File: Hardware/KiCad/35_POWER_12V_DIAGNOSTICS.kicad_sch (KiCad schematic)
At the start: 0 parts

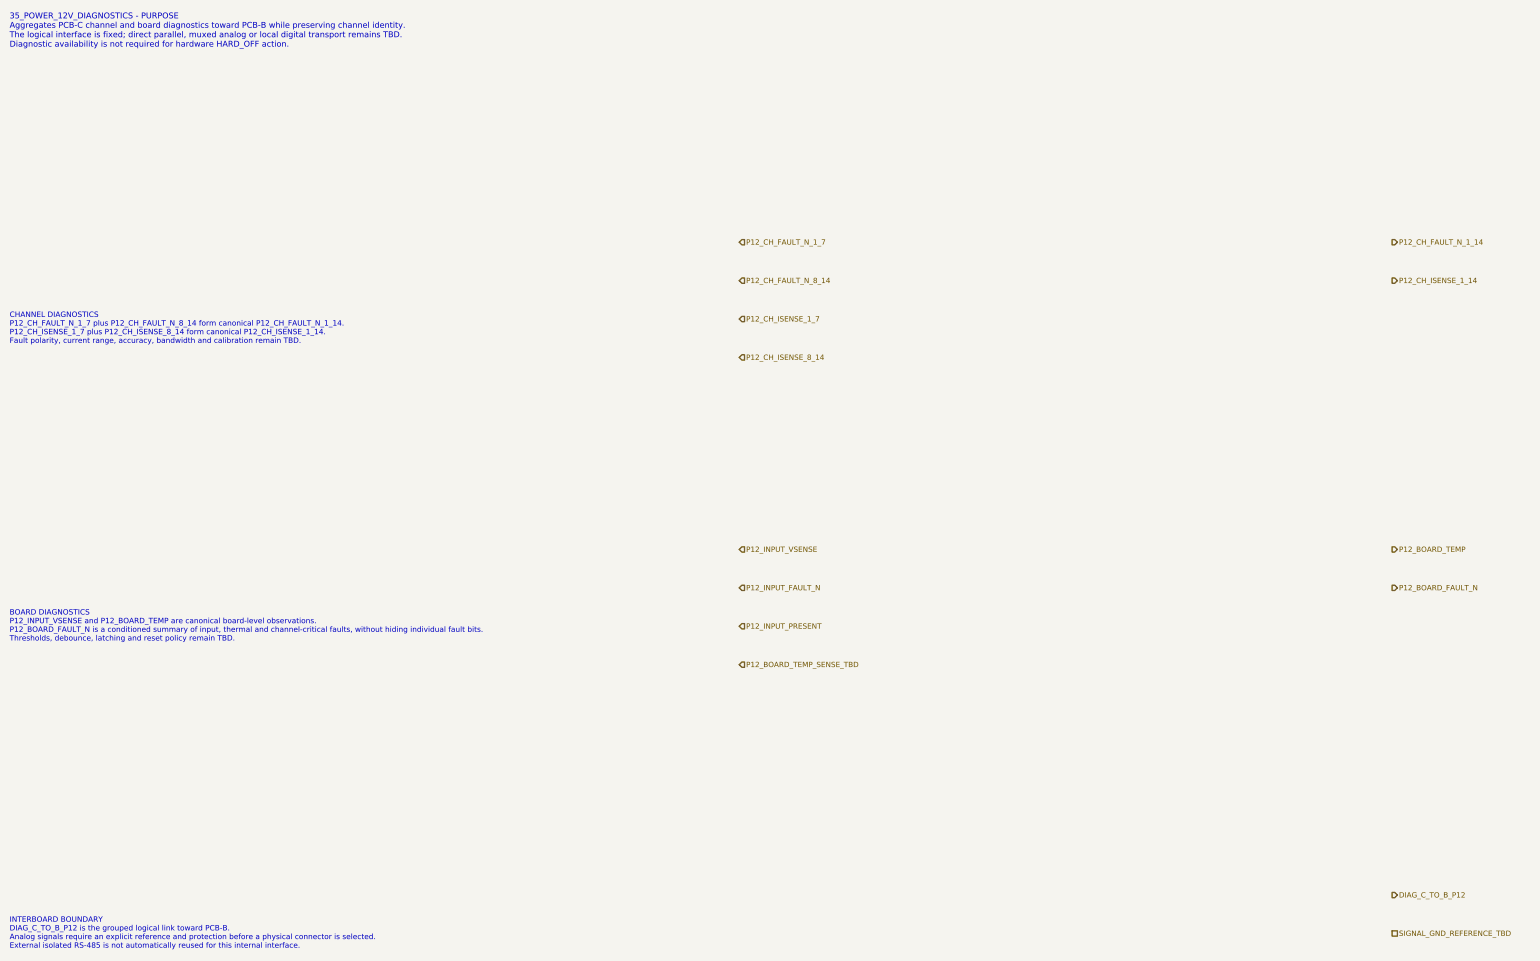
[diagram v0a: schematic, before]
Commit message: hardware: align PCB-C POWER_12V interfaces
Merge PCB-C interface consistency after verifying exact control/diagnostic buses and SAFE/HARD_OFF semantics.
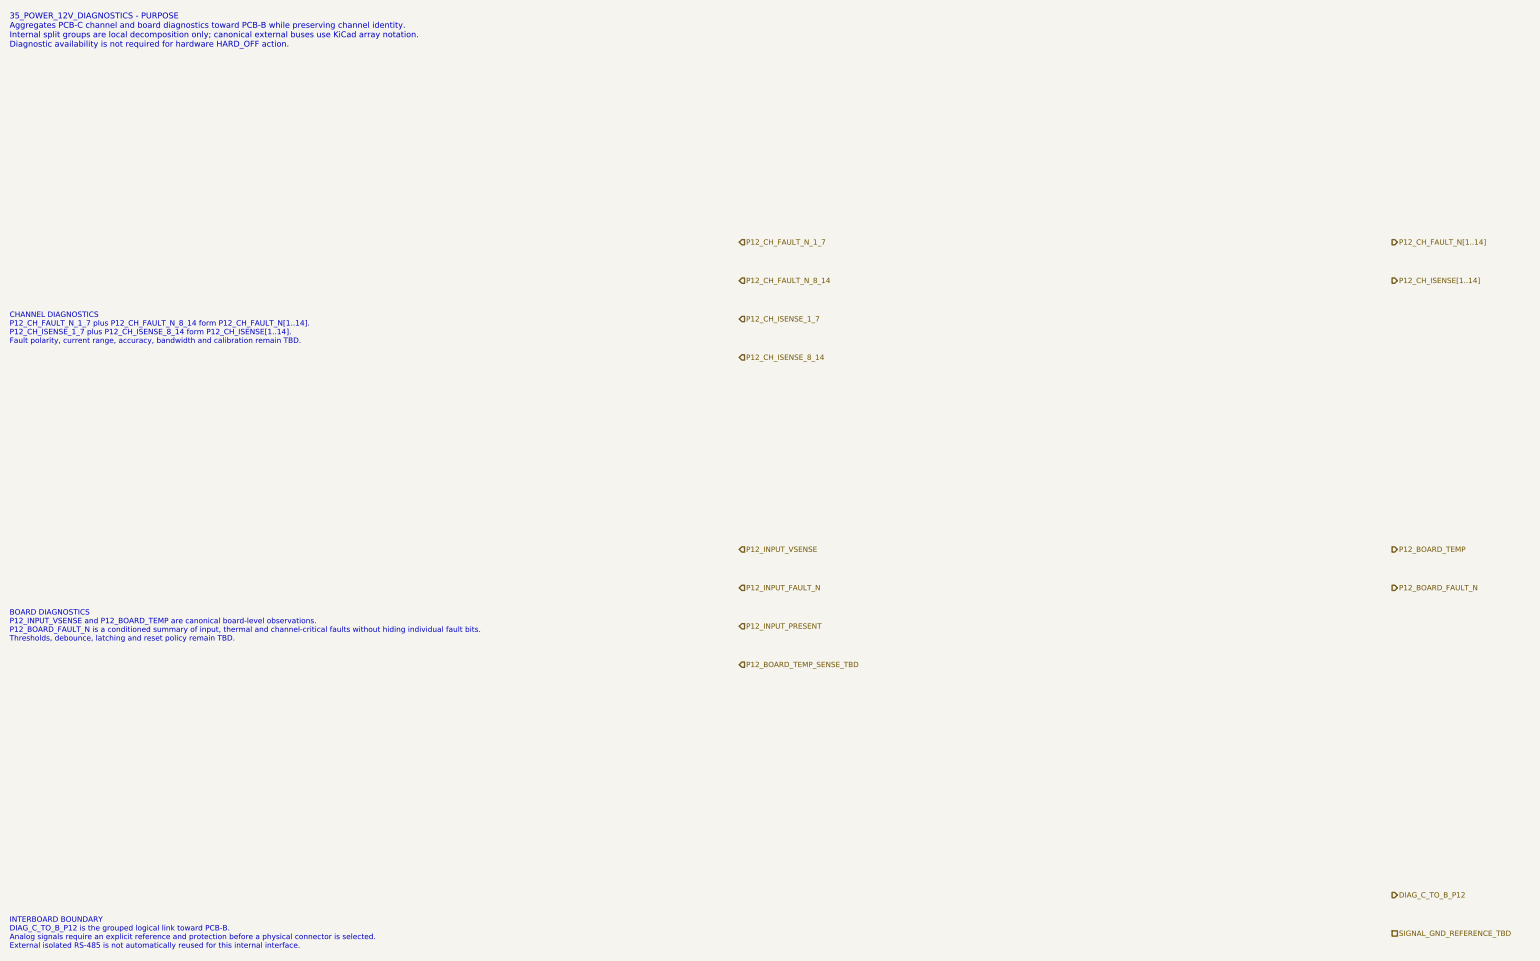
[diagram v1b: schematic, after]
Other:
- note added: "35_POWER_12V_DIAGNOSTICS - PURPOSE Aggregates PCB-C channel and board diagnostics toward PCB-B while preserving channel identity. Internal split groups are local decomposition only; canonical external buses use KiCad array notation. Diagnostic availability is not required for hardware HARD_OFF action."
- note added: "BOARD DIAGNOSTICS P12_INPUT_VSENSE and P12_BOARD_TEMP are canonical board-level observations. P12_BOARD_FAULT_N is a conditioned summary of input, thermal and channel-critical faults without hiding individual fault bits. Thresholds, debounce, latching and reset policy remain TBD."
- note added: "CHANNEL DIAGNOSTICS P12_CH_FAULT_N_1_7 plus P12_CH_FAULT_N_8_14 form P12_CH_FAULT_N[1..14]. P12_CH_ISENSE_1_7 plus P12_CH_ISENSE_8_14 form P12_CH_ISENSE[1..14]. Fault polarity, current range, accuracy, bandwidth and calibration remain TBD."
- note removed: "35_POWER_12V_DIAGNOSTICS - PURPOSE Aggregates PCB-C channel and board diagnostics toward PCB-B while preserving channel identity. The logical interface is fixed; direct parallel, muxed analog or local digital transport remains TBD. Diagnostic availability is not required for hardware HARD_OFF action."
- note removed: "BOARD DIAGNOSTICS P12_INPUT_VSENSE and P12_BOARD_TEMP are canonical board-level observations. P12_BOARD_FAULT_N is a conditioned summary of input, thermal and channel-critical faults, without hiding individual fault bits. Thresholds, debounce, latching and reset policy remain TBD."
- note removed: "CHANNEL DIAGNOSTICS P12_CH_FAULT_N_1_7 plus P12_CH_FAULT_N_8_14 form canonical P12_CH_FAULT_N_1_14. P12_CH_ISENSE_1_7 plus P12_CH_ISENSE_8_14 form canonical P12_CH_ISENSE_1_14. Fault polarity, current range, accuracy, bandwidth and calibration remain TBD."
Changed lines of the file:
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@@
 		(title "35_POWER_12V_DIAGNOSTICS - channel and board diagnostics")
 		(date "2026-07-15")
-		(rev "B0")
+		(rev "B1")
 		(company "Gonoboben/plataVM")
-		(comment 1 "Architecture Level A/B: 14-channel fault/current and board-state aggregation")
+		(comment 1 "Interface consistency: exact P12 diagnostic arrays and board-level ports")
 		(comment 2 "No ADC, mux, local controller, sensor, serializer, isolator or footprint selected")
 	)
-	(text "35_POWER_12V_DIAGNOSTICS - PURPOSE\nAggregates PCB-C channel and board diagnostics toward PCB-B while preserving channel identity.\nThe logical interface is fixed; direct parallel, muxed analog or local digital transport remains TBD.\nDiagnostic availability is not required for hardware HARD_OFF action."
+	(text "35_POWER_12V_DIAGNOSTICS - PURPOSE\nAggregates PCB-C channel and board diagnostics toward PCB-B while preserving channel identity.\nInternal split groups are local decomposition only; canonical external buses use KiCad array notation.\nDiagnostic availability is not required for hardware HARD_OFF action."
 		(exclude_from_sim no)
 		(at 12 14 0)
@@
 		(uuid "power-12v-00000035-0000-4000-8000-000000000101")
 	)
-	(text "CHANNEL DIAGNOSTICS\nP12_CH_FAULT_N_1_7 plus P12_CH_FAULT_N_8_14 form canonical P12_CH_FAULT_N_1_14.\nP12_CH_ISENSE_1_7 plus P12_CH_ISENSE_8_14 form canonical P12_CH_ISENSE_1_14.\nFault polarity, current range, accuracy, bandwidth and calibration remain TBD."
+	(text "CHANNEL DIAGNOSTICS\nP12_CH_FAULT_N_1_7 plus P12_CH_FAULT_N_8_14 form P12_CH_FAULT_N[1..14].\nP12_CH_ISENSE_1_7 plus P12_CH_ISENSE_8_14 form P12_CH_ISENSE[1..14].\nFault polarity, current range, accuracy, bandwidth and calibration remain TBD."
 		(exclude_from_sim no)
 		(at 12 76 0)
@@
 		(uuid "power-12v-00000035-0000-4000-8000-000000000102")
 	)
-	(text "BOARD DIAGNOSTICS\nP12_INPUT_VSENSE and P12_BOARD_TEMP are canonical board-level observations.\nP12_BOARD_FAULT_N is a conditioned summary of input, thermal and channel-critical faults, without hiding individual fault bits.\nThresholds, debounce, latching and reset policy remain TBD."
+	(text "BOARD DIAGNOSTICS\nP12_INPUT_VSENSE and P12_BOARD_TEMP are canonical board-level observations.\nP12_BOARD_FAULT_N is a conditioned summary of input, thermal and channel-critical faults without hiding individual fault bits.\nThresholds, debounce, latching and reset policy remain TBD."
 		(exclude_from_sim no)
 		(at 12 138 0)
@@
 	(hierarchical_label "P12_INPUT_PRESENT" (shape input) (exclude_from_sim no) (at 164 138 0) (effects (font (size 1.1 1.1)) (justify left)) (uuid "power-12v-00000035-0000-4000-8000-000000000207"))
 	(hierarchical_label "P12_BOARD_TEMP_SENSE_TBD" (shape input) (exclude_from_sim no) (at 164 146 0) (effects (font (size 1.1 1.1)) (justify left)) (uuid "power-12v-00000035-0000-4000-8000-000000000208"))
-	(hierarchical_label "P12_CH_FAULT_N_1_14" (shape output) (exclude_from_sim no) (at 300 58 0) (effects (font (size 1.1 1.1)) (justify left)) (uuid "power-12v-00000035-0000-4000-8000-000000000209"))
-	(hierarchical_label "P12_CH_ISENSE_1_14" (shape output) (exclude_from_sim no) (at 300 66 0) (effects (font (size 1.1 1.1)) (justify left)) (uuid "power-12v-00000035-0000-4000-8000-000000000210"))
+	(hierarchical_label "P12_CH_FAULT_N[1..14]" (shape output) (exclude_from_sim no) (at 300 58 0) (effects (font (size 1.1 1.1)) (justify left)) (uuid "power-12v-00000035-0000-4000-8000-000000000209"))
+	(hierarchical_label "P12_CH_ISENSE[1..14]" (shape output) (exclude_from_sim no) (at 300 66 0) (effects (font (size 1.1 1.1)) (justify left)) (uuid "power-12v-00000035-0000-4000-8000-000000000210"))
 	(hierarchical_label "P12_BOARD_TEMP" (shape output) (exclude_from_sim no) (at 300 122 0) (effects (font (size 1.1 1.1)) (justify left)) (uuid "power-12v-00000035-0000-4000-8000-000000000211"))
 	(hierarchical_label "P12_BOARD_FAULT_N" (shape output) (exclude_from_sim no) (at 300 130 0) (effects (font (size 1.1 1.1)) (justify left)) (uuid "power-12v-00000035-0000-4000-8000-000000000212"))
